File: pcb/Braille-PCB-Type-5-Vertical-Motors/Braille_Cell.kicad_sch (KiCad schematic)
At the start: 43 parts, among them U10 AD116, U11 AD116, U12 AD116, U13 AD116, U8 AD116, U9 AD116

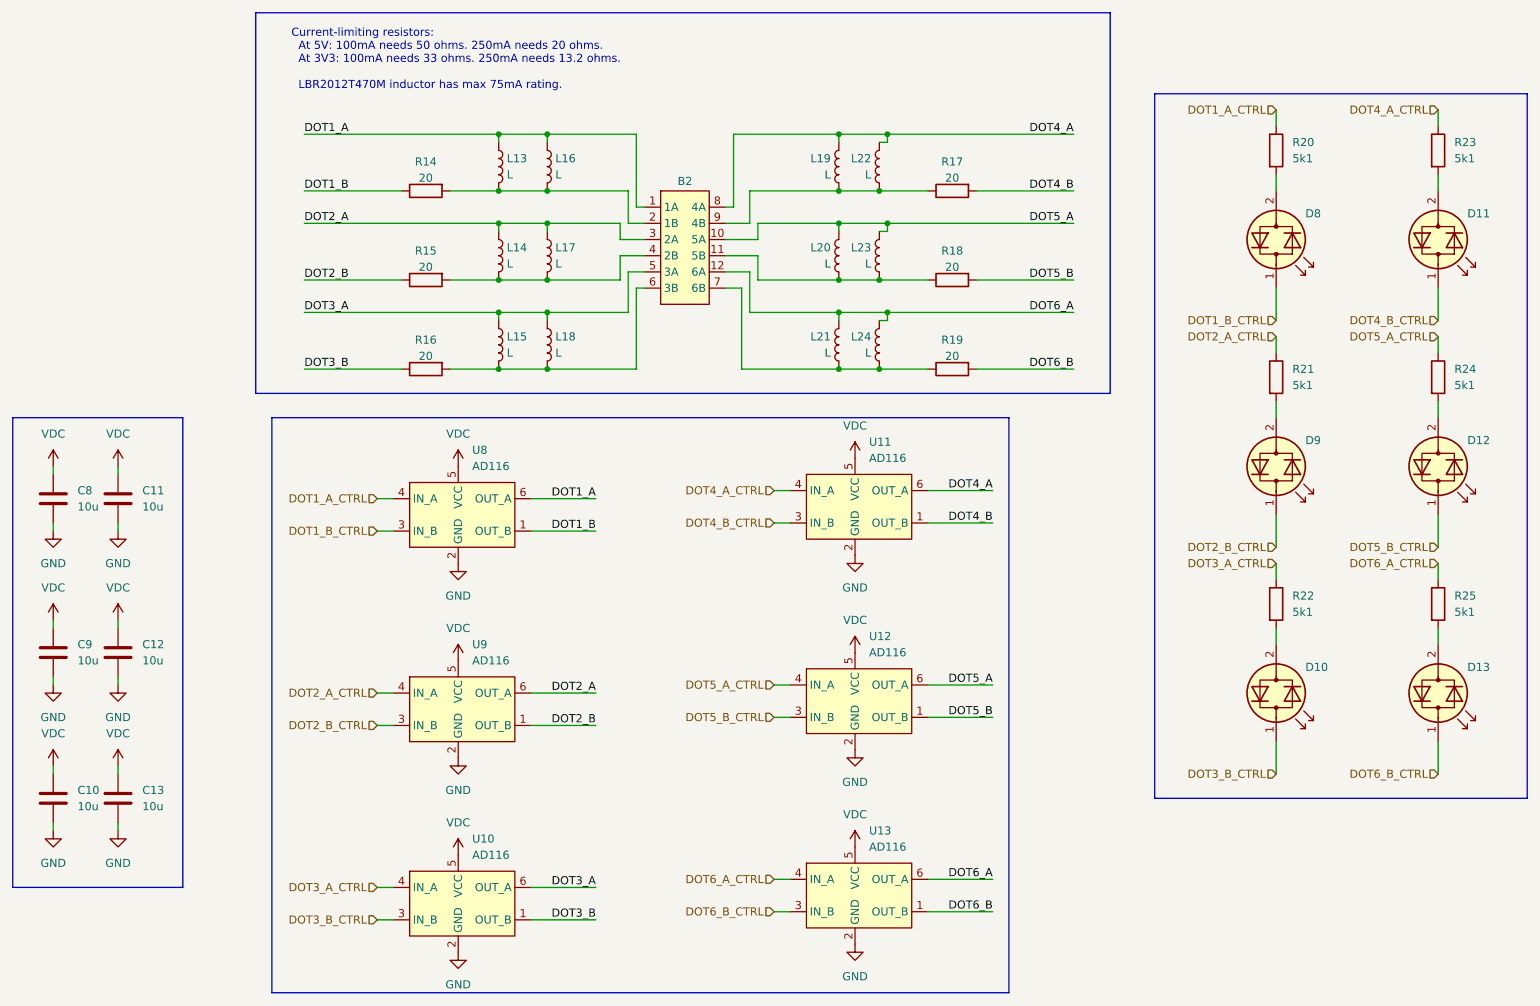
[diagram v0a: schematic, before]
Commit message: PCB: Update to have 3 motors, dimensioned layout template
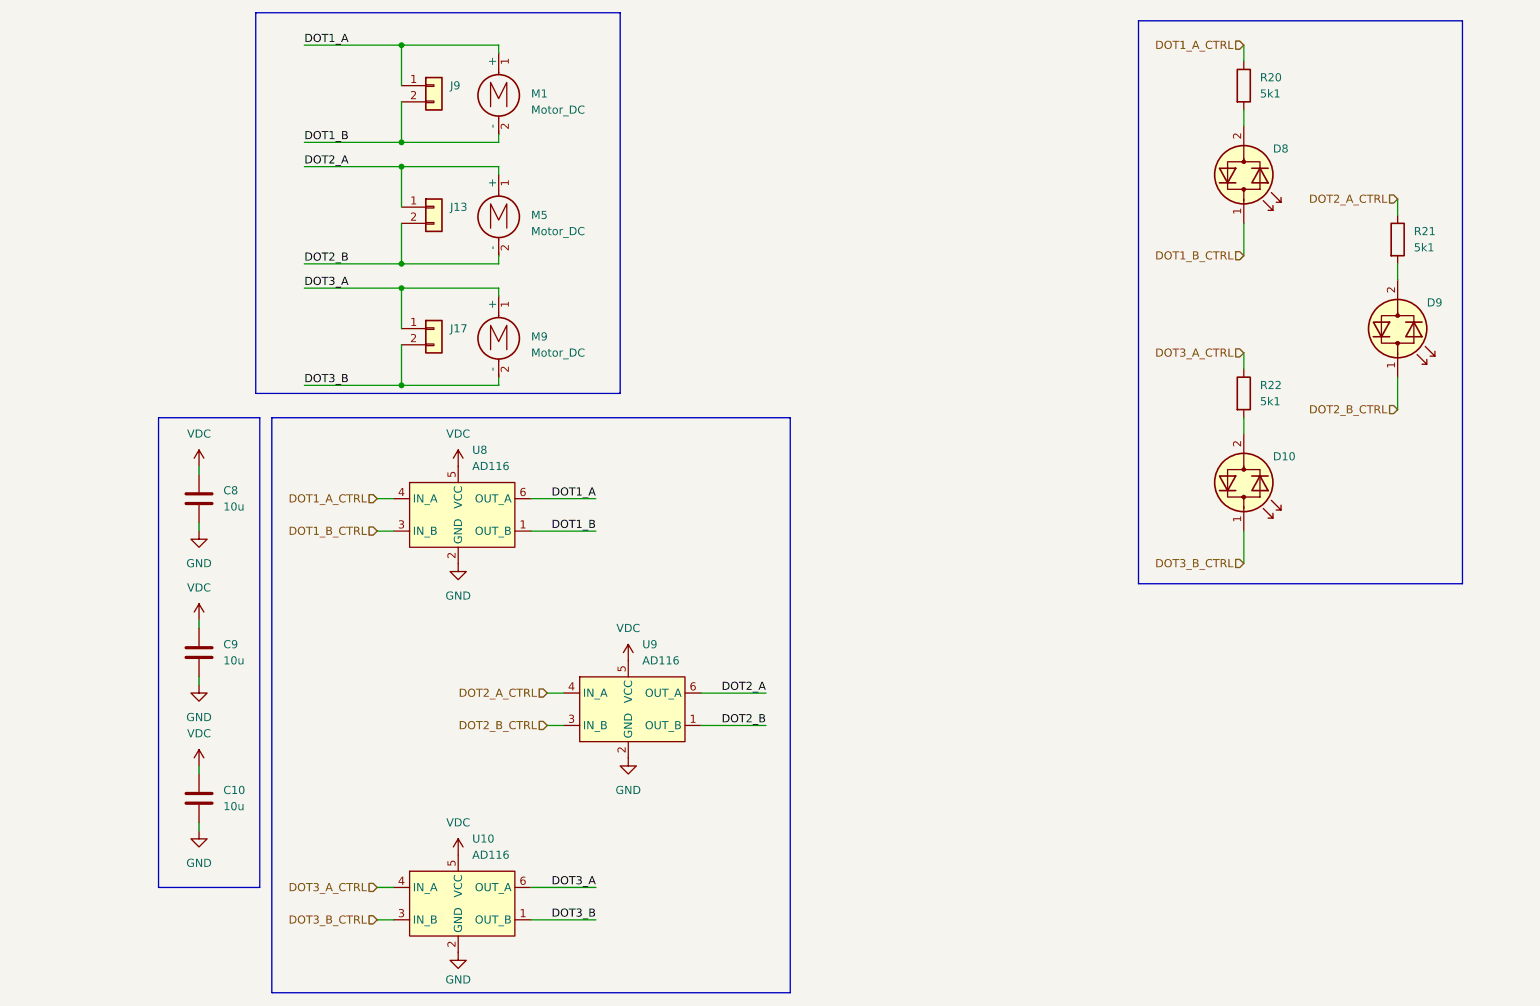
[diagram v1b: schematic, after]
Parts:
- removed B2: ~, 00-project-footprints:Braille_Cell_Breakout, symbol 00-project-symbols:Braille_Cell_Breakout
- removed C11, C12, C13: 10u, Capacitor_SMD:C_1206_3216Metric_Pad1.33x1.80mm_HandSolder, symbol Device:C
- removed D11, D12, D13: LED_Dual_Bidirectional, 00-project-footprints:LED_0603_1608Metric_HandSolder_2x_Reverse, symbol Device:LED_Dual_Bidirectional
- removed L13, L14, L15, L22, L23, L24: L, 00-project-footprints:Inductor_0805_2012Metric_SMD_Vertical_Square_Rev2_1.3mm, symbol Device:L
- removed L16, L17, L18, L19, L20, L21: L, 00-project-footprints:Inductor_VLS201612CX, symbol Device:L
- removed R14, R15, R16, R17, R18, R19: 20, Resistor_SMD:R_0603_1608Metric_Pad0.98x0.95mm_HandSolder, symbol Device:R
- removed R23, R24, R25: 5k1, Resistor_SMD:R_0603_1608Metric_Pad0.98x0.95mm_HandSolder, symbol Device:R
- removed U11, U12, U13: AD116, Package_TO_SOT_SMD:SOT-23-6, symbol 00-project-symbols:AD116_H_Bridge
- added J13, J17, J9: Conn_01x02, 00-project-footprints:PinHeader_1x02_P2.54mm_Vertical_Tight_Centered, symbol Connector_Generic:Conn_01x02
- added M1, M5, M9: Motor_DC, 00-project-footprints:Motor_Tiny_0408_Vertical, symbol Motor:Motor_DC
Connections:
- net DOT1_A: now also J9.1 (Pin_1), M1.1 (+)
- net DOT1_B: now also J9.2 (Pin_2), M1.2 (-)
- net DOT2_A: now also J13.1 (Pin_1), M5.1 (+)
- net DOT2_B: now also J13.2 (Pin_2), M5.2 (-)
- net DOT3_A: now also J17.1 (Pin_1), M9.1 (+)
- net DOT3_B: now also J17.2 (Pin_2), M9.2 (-)
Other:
- note removed: "Current-limiting resistors: At 5V: 100mA needs 50 ohms. 250mA needs 20 ohms. At 3V3: 100mA needs 33 ohms. 250mA needs 13.2 ohms. LBR2012T470M inductor has max 75mA rating."
- moved on the sheet: C10, C8, C9, D10, D8, D9, R20, R21, R22, U9

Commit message: PCB WIP: Add motor shaft holes
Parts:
- added H13, H17, H21: MountingHole, 00-project-footprints:Hole_for_Motor_Shaft, symbol Mechanical:MountingHole
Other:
- note added: "Motor shafts from lower layer."

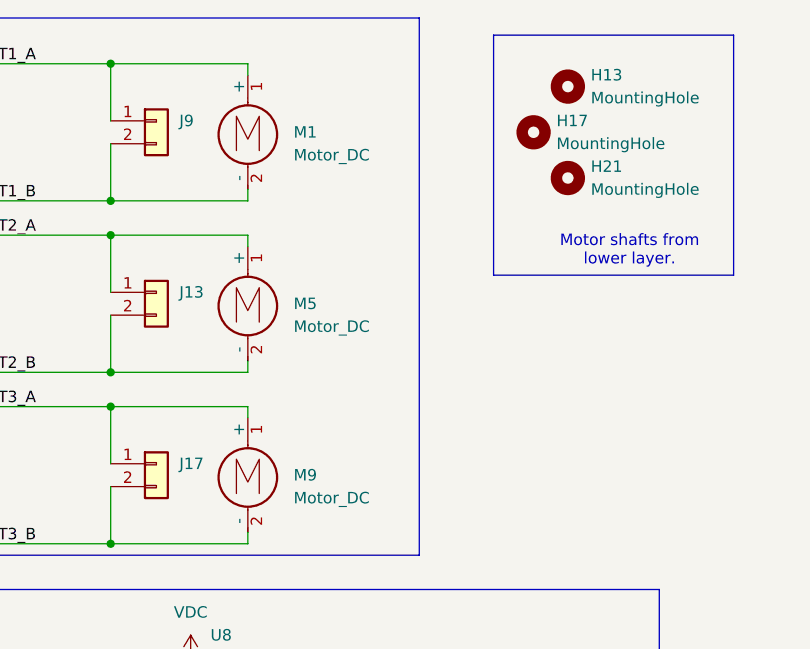
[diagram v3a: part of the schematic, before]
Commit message: PCB Rev 2: Increase shaft hole diameter from 1mm to 2mm
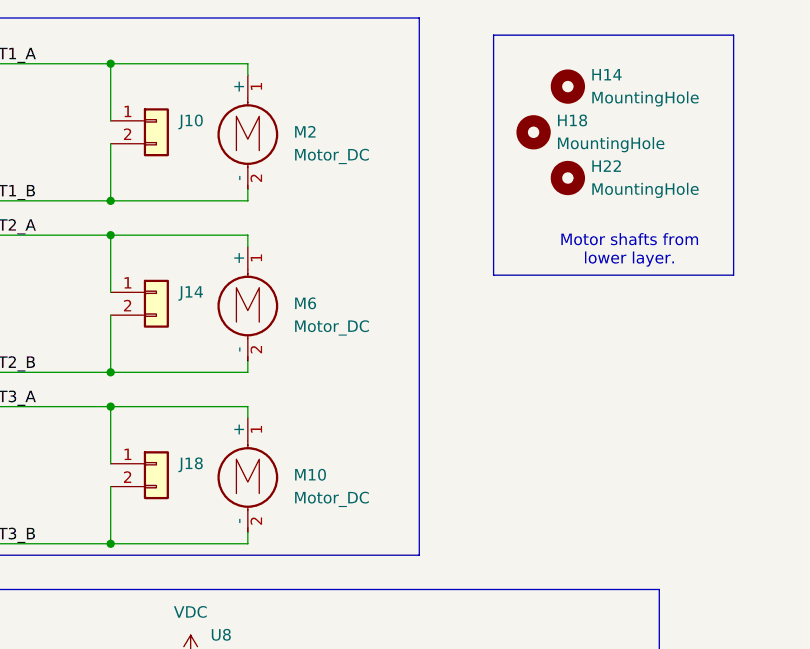
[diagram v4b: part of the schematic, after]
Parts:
- renumbered H13 to H14, H17 to H18, H21 to H22, J9 to J10, J13 to J14, J17 to J18, M9 to M10, M1 to M2, M5 to M6
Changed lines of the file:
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@@
 	(paper "USLetter")
 	(title_block
-		(date "2025-01-10")
-		(rev "Type 5 Rev 1")
+		(date "2025-01-11")
+		(rev "Type 5 Rev 2")
 	)
 	(junction
@@
 		(dnp no)
 		(fields_autoplaced yes)
-		(property "Reference" "H21"
+		(property "Reference" "H22"
 			(at 132.08 30.4799 0)
 			(effects
@@
 		(dnp no)
 		(fields_autoplaced yes)
-		(property "Reference" "M5"
+		(property "Reference" "M6"
 			(at 99.06 45.7199 0)
 			(effects
@@
 		(dnp no)
 		(fields_autoplaced yes)
-		(property "Reference" "M1"
+		(property "Reference" "M2"
 			(at 99.06 26.6699 0)
 			(effects
@@
 		(dnp no)
 		(fields_autoplaced yes)
-		(property "Reference" "H17"
+		(property "Reference" "H18"
 			(at 128.27 25.3999 0)
 			(effects
@@
 		(dnp no)
 		(fields_autoplaced yes)
-		(property "Reference" "H13"
+		(property "Reference" "H14"
 			(at 132.08 20.3199 0)
 			(effects
@@
 		(dnp no)
 		(fields_autoplaced yes)
-		(property "Reference" "J9"
+		(property "Reference" "J10"
 			(at 86.36 25.3999 0)
 			(effects
@@
 		(dnp no)
 		(fields_autoplaced yes)
-		(property "Reference" "M9"
+		(property "Reference" "M10"
 			(at 99.06 64.7699 0)
 			(effects
@@
 		(dnp no)
 		(fields_autoplaced yes)
-		(property "Reference" "J17"
+		(property "Reference" "J18"
 			(at 86.36 63.4999 0)
 			(effects
@@
 		(dnp no)
 		(fields_autoplaced yes)
-		(property "Reference" "J13"
+		(property "Reference" "J14"
 			(at 86.36 44.4499 0)
 			(effects
